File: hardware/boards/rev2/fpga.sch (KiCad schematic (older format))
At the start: 73 parts, among them J1 SD_Card, P1 CONN_02X04, P2 CONN_02X04, Q1 DNP(RE1C002UN), SW1 SW_PUSH, U6 XC7A15T-FTG256, U7 W25Q32JV

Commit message: reorganize schematic
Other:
- note added: "20 (0) mA"
- note added: "201 (1) mA"
- note added: "215 (95) mA"
- note added: "220 mA"
- note added: "3V6: 95 (78) mA\n3V3: 3 mA"
- note added: "62 (2) mA"
- note added: "62 (22) mA"
- note removed: "5 mA"
- note removed: "70 mA"
- note removed: "78 mA"
- note removed: "Iq: 1 mA\nIon: 201 mA"
- note removed: "Iq: 10 uA\nIon: 20 mA"
- note removed: "Iq: 2 mA\nIon: 62 mA"
- note removed: "Iq: 22 mA\nIon: 62 mA"
- note removed: "Iq: 95 mA\nIon: 215 mA"
- note removed: "Power-on current\n1V0: 277 mA\n1V8: 62 mA\n3V3: 296 mA\n3V6: 78 mA"
- note removed: "Quiescent current\n1V0: 97 mA\n1V8: 22 mA\n3V3: 71 mA\n3V6: 78 mA"
- moved on the sheet: C14, C15, C16, C17, C18, C19, C20, C21, C22, C23, C24, C25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

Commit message: revert to kicad v5 for pcb gen
V6 contains a few bugs and a V6 board cannot be edited with V5.
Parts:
- removed P1, P2: CONN_02X04, Connector_PinHeader_2.54mm:PinHeader_2x04_P2.54mm_Vertical_SMD, symbol Connector_Generic:Conn_02x04_Odd_Even
- added J6: Conn_02x08_Odd_Even, Connector_PinHeader_1.27mm:PinHeader_2x08_P1.27mm_Vertical, symbol Connector_Generic:Conn_02x08_Odd_Even
- U6: footprint fmcw:FTG256 -> Package_BGA:Xilinx_FTG256
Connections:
- net 3V3D: now also J6.10 (Pin_10), J6.2 (Pin_2)
- net EXT1_1: now also J6.3 (Pin_3)
- net EXT1_2: now also J6.5 (Pin_5)
- net EXT1_3: now also J6.7 (Pin_7)
- net EXT1_4: now also J6.4 (Pin_4)
- net EXT1_5: now also J6.6 (Pin_6)
- net EXT1_6: now also J6.8 (Pin_8)
- net EXT2_1: now also J6.11 (Pin_11)
- net EXT2_2: now also J6.13 (Pin_13)
- net EXT2_3: now also J6.15 (Pin_15)
- net EXT2_4: now also J6.12 (Pin_12)
- net EXT2_5: now also J6.14 (Pin_14)
- net EXT2_6: now also J6.16 (Pin_16)
- net GND: now also J6.1 (Pin_1), J6.9 (Pin_9)
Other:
- note added: "3"
- note added: "4"
- note removed: "VCCO"
- moved on the sheet: C15, C16, C20, C21, C22, C23, C24, C25, C26, C27, C28, C29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

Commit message: finish placement and routing
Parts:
- removed C15: 470n, Capacitor_SMD:C_0603_1608Metric, symbol Device:C
- J6: footprint Connector_PinHeader_1.27mm:PinHeader_2x08_P1.27mm_Vertical -> Connector_PinHeader_2.54mm:PinHeader_2x07_P2.54mm_Vertical; symbol Connector_Generic:Conn_02x08_Odd_Even -> Connector_Generic:Conn_02x07_Odd_Even
- TP1, TP2, TP3, TP4, TP5, TP6, TP7, TP8, TP9: footprint TestPoint:TestPoint_Pad_D1.0mm -> TestPoint:TestPoint_Loop_D1.80mm_Drill1.0mm_Beaded
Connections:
- net 3V3D: no longer J6.10 (Pin_10)
- net EXT2_1: now also J6.9 (Pin_9); no longer J6.11 (Pin_11)
- net EXT2_2: now also J6.11 (Pin_11); no longer J6.13 (Pin_13)
- net EXT2_3: now also J6.13 (Pin_13); no longer J6.15 (Pin_15)
- net EXT2_4: now also J6.10 (Pin_10); no longer J6.12 (Pin_12)
- net EXT2_5: now also J6.12 (Pin_12); no longer J6.14 (Pin_14)
- net EXT2_6: now also J6.14 (Pin_14); no longer J6.16 (Pin_16)
- net GND: no longer J6.9 (Pin_9)
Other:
- moved on the sheet: R10
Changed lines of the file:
@@
 	1550 14050 1550 14000
 Wire Wire Line
-	1550 14400 2100 14400
-Wire Wire Line
-	1550 14450 1550 14400
-Wire Wire Line
 	1750 10100 1550 10100
 Wire Wire Line
@@
 	2100 14300 2000 14300
 Wire Wire Line
+	2100 14400 2000 14400
+Wire Wire Line
 	2100 14500 2000 14500
 Wire Wire Line
 	2100 14600 2000 14600
 Wire Wire Line
-	2100 14700 2000 14700
-Wire Wire Line
 	2200 10300 2200 10500
 Wire Wire Line
@@
 	2600 14300 2700 14300
 Wire Wire Line
-	2600 14400 3200 14400
+	2600 14400 2700 14400
 Wire Wire Line
 	2600 14500 2700 14500
@@
 	2600 14600 2700 14600
 Wire Wire Line
-	2600 14700 2700 14700
-Wire Wire Line
 	2650 1950 2550 1950
 Wire Wire Line
@@
 	2650 6250 2400 6250
 Wire Wire Line
-	3200 14400 3200 14450
-Wire Wire Line
 	3500 14000 3500 14050
 Wire Wire Line
@@
 	5050 14750 5050 14950
 Wire Wire Line
-	6300 13850 6300 13950
+	14150 11550 14150 11650
 Wire Wire Line
 	6950 15100 6900 15100
@@
 Text Label 2000 14300 2    60   ~ 0
 EXT1_3
+Text Label 2000 14400 2    60   ~ 0
+EXT2_1
 Text Label 2000 14500 2    60   ~ 0
-EXT2_1
+EXT2_2
 Text Label 2000 14600 2    60   ~ 0
-EXT2_2
-Text Label 2000 14700 2    60   ~ 0
 EXT2_3
 Text Label 2050 10200 0    60   ~ 0
@@
 Text Label 2700 14300 0    60   ~ 0
 EXT1_6
+Text Label 2700 14400 0    60   ~ 0
+EXT2_4
 Text Label 2700 14500 0    60   ~ 0
-EXT2_4
+EXT2_5
 Text Label 2700 14600 0    60   ~ 0
-EXT2_5
-Text Label 2700 14700 0    60   ~ 0
 EXT2_6
-Text Label 3050 14400 0    60   ~ 0
-3V3D
 Text Label 3250 14000 0    60   ~ 0
 3V3D
@@
 Text Label 5050 14150 2    60   ~ 0
 PROGRAM_B
-Text Label 6300 13550 0    60   ~ 0
-3V3D
-Text Label 6300 13950 0    60   ~ 0
+Text Label 14150 11250 0    60   ~ 0
+3V3D
+Text Label 14150 11650 0    60   ~ 0
 INIT_B
 Text Label 7200 1000 0    60   ~ 0
@@
 F 0 "TP1" H 7250 2925 50  0000 C CNN
 F 1 "TestPoint" H 7250 2834 50  0000 C CNN
-F 2 "TestPoint:TestPoint_Pad_D1.0mm" H 7450 2600 50  0001 C CNN
+F 2 "TestPoint:TestPoint_Loop_D1.80mm_Drill1.0mm_Beaded" H 7450 2600 50  0001 C CNN
 F 3 "~" H 7450 2600 50  0001 C CNN
 	1    7250 2600
@@
 F 0 "TP2" H 7550 2825 50  0000 C CNN
 F 1 "TestPoint" H 7550 2734 50  0000 C CNN
-F 2 "TestPoint:TestPoint_Pad_D1.0mm" H 7750 2500 50  0001 C CNN
+F 2 "TestPoint:TestPoint_Loop_D1.80mm_Drill1.0mm_Beaded" H 7750 2500 50  0001 C CNN
 F 3 "~" H 7750 2500 50  0001 C CNN
 	1    7550 2500
@@
 F 0 "TP3" H 12300 10575 50  0000 C CNN
 F 1 "TestPoint" H 12300 10484 50  0000 C CNN
-F 2 "TestPoint:TestPoint_Pad_D1.0mm" H 12500 10250 50  0001 C CNN
+F 2 "TestPoint:TestPoint_Loop_D1.80mm_Drill1.0mm_Beaded" H 12500 10250 50  0001 C CNN
 F 3 "~" H 12500 10250 50  0001 C CNN
 	1    12300 10250
@@
 F 0 "TP4" H 12600 10675 50  0000 C CNN
 F 1 "TestPoint" H 12600 10584 50  0000 C CNN
-F 2 "TestPoint:TestPoint_Pad_D1.0mm" H 12800 10350 50  0001 C CNN
+F 2 "TestPoint:TestPoint_Loop_D1.80mm_Drill1.0mm_Beaded" H 12800 10350 50  0001 C CNN
 F 3 "~" H 12800 10350 50  0001 C CNN
 	1    12600 10350
@@
 F 0 "TP5" H 12900 10775 50  0000 C CNN
 F 1 "TestPoint" H 12900 10684 50  0000 C CNN
-F 2 "TestPoint:TestPoint_Pad_D1.0mm" H 13100 10450 50  0001 C CNN
+F 2 "TestPoint:TestPoint_Loop_D1.80mm_Drill1.0mm_Beaded" H 13100 10450 50  0001 C CNN
 F 3 "~" H 13100 10450 50  0001 C CNN
 	1    12900 10450
@@
 F 0 "TP6" H 13200 10875 50  0000 C CNN
 F 1 "TestPoint" H 13200 10784 50  0000 C CNN
-F 2 "TestPoint:TestPoint_Pad_D1.0mm" H 13400 10550 50  0001 C CNN
+F 2 "TestPoint:TestPoint_Loop_D1.80mm_Drill1.0mm_Beaded" H 13400 10550 50  0001 C CNN
 F 3 "~" H 13400 10550 50  0001 C CNN
 	1    13200 10550
@@
 F 0 "TP7" H 13250 11575 50  0000 C CNN
 F 1 "TestPoint" H 13250 11484 50  0000 C CNN
-F 2 "TestPoint:TestPoint_Pad_D1.0mm" H 13450 11250 50  0001 C CNN
+F 2 "TestPoint:TestPoint_Loop_D1.80mm_Drill1.0mm_Beaded" H 13450 11250 50  0001 C CNN
 F 3 "~" H 13450 11250 50  0001 C CNN
 	1    13250 11250
@@
 F 0 "TP8" H 13500 11075 50  0000 C CNN
 F 1 "TestPoint" H 13500 10984 50  0000 C CNN
-F 2 "TestPoint:TestPoint_Pad_D1.0mm" H 13700 10750 50  0001 C CNN
+F 2 "TestPoint:TestPoint_Loop_D1.80mm_Drill1.0mm_Beaded" H 13700 10750 50  0001 C CNN
 F 3 "~" H 13700 10750 50  0001 C CNN
 	1    13500 10750
@@
 F 0 "TP9" H 20758 4370 50  0000 L CNN
 F 1 "TestPoint" H 20758 4279 50  0000 L CNN
-F 2 "TestPoint:TestPoint_Pad_D1.0mm" H 20900 4250 50  0001 C CNN
+F 2 "TestPoint:TestPoint_Loop_D1.80mm_Drill1.0mm_Beaded" H 20900 4250 50  0001 C CNN
 F 3 "~" H 20900 4250 50  0001 C CNN
 	1    20700 4250
@@
 $EndComp
 $Comp
-L power:GND #PWR024
-U 1 1 596CB067
-P 1550 14450
-F 0 "#PWR024" H 1550 14200 50  0001 C CNN
-F 1 "GND" H 1550 14300 50  0000 C CNN
-F 2 "" H 1550 14450 60  0000 C CNN
-F 3 "" H 1550 14450 60  0000 C CNN
-	1    1550 14450
-	1    0    0    -1
-$EndComp
-$Comp
 L power:GND #PWR025
 U 1 1 5FFB0BA7
@@
 F 3 "" H 2250 12400 50  0001 C CNN
 	1    2250 12400
-	1    0    0    -1
-$EndComp
-$Comp
-L power:GND #PWR027
-U 1 1 59728463
-P 3200 14750
-F 0 "#PWR027" H 3200 14500 50  0001 C CNN
-F 1 "GND" H 3200 14600 50  0000 C CNN
-F 2 "" H 3200 14750 60  0000 C CNN
-F 3 "" H 3200 14750 60  0000 C CNN
-	1    3200 14750
 	1    0    0    -1
 $EndComp
@@
 L Device:R R10
 U 1 1 58563673
-P 6300 13700
-F 0 "R10" H 6370 13746 50  0000 L CNN
-F 1 "4.7k" H 6370 13655 50  0000 L CNN
-F 2 "Resistor_SMD:R_0402_1005Metric" V 6230 13700 30  0001 C CNN
-F 3 "" H 6300 13700 30  0000 C CNN
-F 4 "" H 2150 3900 50  0001 C CNN "MFN"
-	1    6300 13700
+P 14150 11400
+F 0 "R10" H 14220 11446 50  0000 L CNN
+F 1 "4.7k" H 14220 11355 50  0000 L CNN
+F 2 "Resistor_SMD:R_0402_1005Metric" V 14080 11400 30  0001 C CNN
+F 3 "" H 14150 11400 30  0000 C CNN
+F 4 "" H 10000 1600 50  0001 C CNN "MFN"
+	1    14150 11400
 	1    0    0    -1
 $EndComp
@@
 $EndComp
 $Comp
-L Device:C C15
-U 1 1 59727E70
-P 3200 14600
-F 0 "C15" H 3225 14700 50  0000 L CNN
-F 1 "470n" H 3225 14500 50  0000 L CNN
-F 2 "Capacitor_SMD:C_0603_1608Metric" H 3238 14450 30  0001 C CNN
-F 3 "" H 3200 14600 60  0000 C CNN
-F 4 "" H 1100 3900 50  0001 C CNN "MFN"
-	1    3200 14600
-	1    0    0    -1
-$EndComp
-$Comp
 L Device:C C16
 U 1 1 59728DD2
@@
 $EndComp
 $Comp
-L Connector_Generic:Conn_02x08_Odd_Even J6
+L Connector_Generic:Conn_02x07_Odd_Even J6
 U 1 1 5EAD300D
 P 2300 14300
 F 0 "J6" H 2350 14816 50  0000 C CNN
 F 1 "Conn_02x08_Odd_Even" H 2350 14725 50  0000 C CNN
-F 2 "Connector_PinHeader_1.27mm:PinHeader_2x08_P1.27mm_Vertical" H 2300 14300 50  0001 C CNN
+F 2 "Connector_PinHeader_2.54mm:PinHeader_2x07_P2.54mm_Vertical" H 2300 14300 50  0001 C CNN
 F 3 "~" H 2300 14300 50  0001 C CNN
 	1    2300 14300

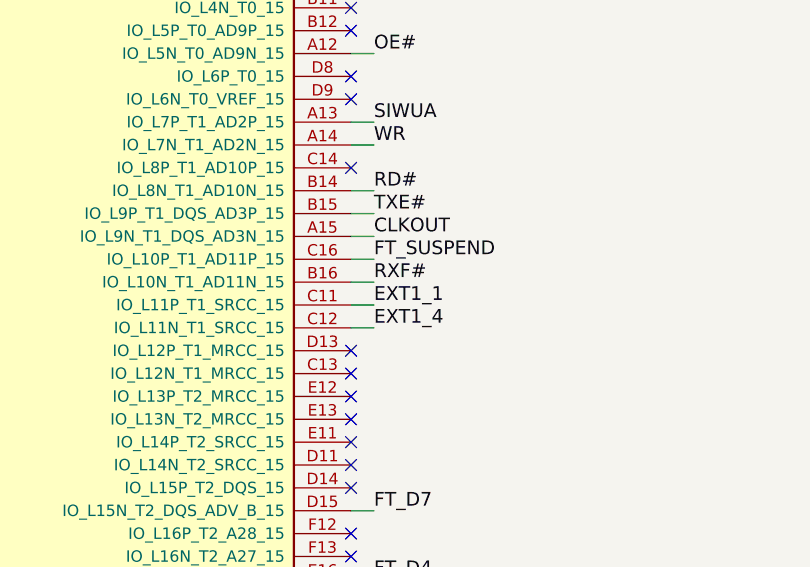
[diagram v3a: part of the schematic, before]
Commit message: switch ftclk to MRCC pin and place silkscreen
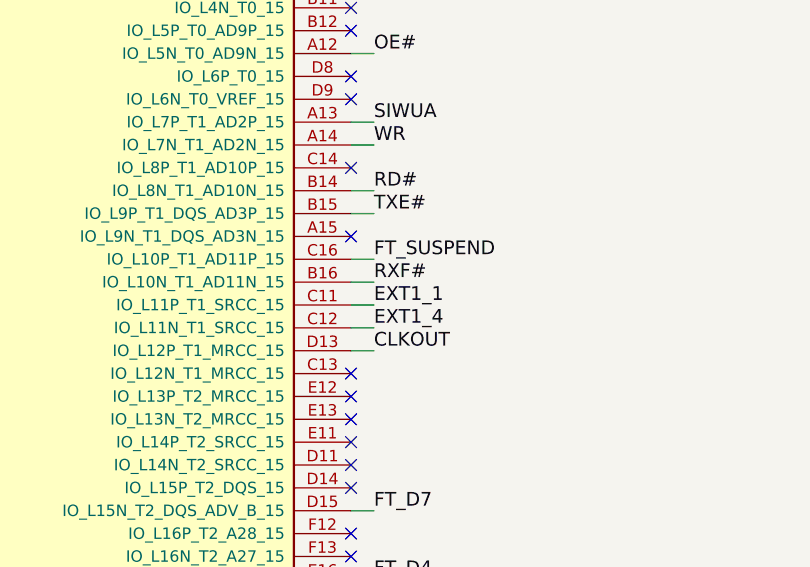
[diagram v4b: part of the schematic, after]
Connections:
- net CLKOUT: now also U6.D13 (IO_L12P_T1_MRCC_15); no longer U6.A15 (IO_L9N_T1_DQS_AD3N_15)
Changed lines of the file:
@@
 Connection ~ 7250 15300
 Connection ~ 7300 3350
-Connection ~ 11750 1700
-Connection ~ 11650 1700
-Connection ~ 11550 1700
-Connection ~ 11450 1700
-Connection ~ 11350 1700
-Connection ~ 9150 1700
-Connection ~ 9050 1700
-Connection ~ 8950 1700
-Connection ~ 8850 1700
-Connection ~ 8750 1700
 Connection ~ 16850 11850
 Connection ~ 16000 11850
@@
 NoConn ~ 12250 2500
 NoConn ~ 12250 5300
-NoConn ~ 12250 4800
 NoConn ~ 12250 5400
 NoConn ~ 12250 5200
@@
 	8550 1400 8700 1400
 Wire Wire Line
-	8650 1700 8750 1700
-Wire Wire Line
 	8700 1000 8700 1050
 Wire Wire Line
@@
 	8700 1400 8950 1400
 Wire Wire Line
-	8750 1700 8850 1700
-Wire Wire Line
-	8850 1700 8950 1700
-Wire Wire Line
 	8950 1000 8950 1050
 Wire Wire Line
 	8950 1350 8950 1400
 Wire Wire Line
-	8950 1700 9050 1700
-Wire Wire Line
-	9050 1700 9150 1700
-Wire Wire Line
-	9150 1700 11350 1700
-Wire Wire Line
 	9750 14450 9950 14450
 Wire Wire Line
@@
 	11300 14000 11300 14050
 Wire Wire Line
-	11350 1700 11450 1700
-Wire Wire Line
-	11450 1700 11550 1700
-Wire Wire Line
-	11550 1700 11650 1700
-Wire Wire Line
-	11650 1700 11750 1700
-Wire Wire Line
 	11700 9550 12050 9550
 Wire Wire Line
-	11750 1700 11850 1700
-Wire Wire Line
 	11800 1000 11800 1050
 Wire Wire Line
@@
 Wire Wire Line
 	12250 3800 12350 3800
-Wire Wire Line
-	12250 4300 12350 4300
 Wire Wire Line
 	12250 4700 12350 4700
@@
 Text Label 12350 4200 0    60   ~ 0
 TXE#
-Text Label 12350 4300 0    60   ~ 0
+Text Label 12350 4800 0    60   ~ 0
 CLKOUT
 Text Label 12350 4400 0    60   ~ 0
@@
 $Comp
 L FPGA_Xilinx_Artix7:XC7A15T-FTG256 U?
-U 1 1 5B9D6CE1
-P 10250 4600
-AR Path="/5B9D6CE1" Ref="U?"  Part="1"
-AR Path="/59395D6A/5B9D6CE1" Ref="U6"  Part="1"
-F 0 "U6" H 10250 4600 50  0000 C CNN
-F 1 "XC7A15T-FTG256" H 10250 1535 50  0000 C CNN
-F 2 "Package_BGA:Xilinx_FTG256" H 10250 4600 50  0001 C CNN
-F 3 "" H 10250 4600 50  0000 C CNN
-F 4 "XC7A15T-1FTG256C" H 3900 1100 50  0001 C CNN "MFN"
-	1    10250 4600
-	1    0    0    -1
-$EndComp
-$Comp
-L FPGA_Xilinx_Artix7:XC7A15T-FTG256 U?
 U 2 1 5CE2C3EB
 P 17800 4850
@@
 F22 "SUSPEND" O L 2650 2800 60
 $EndSheet
+Connection ~ 11750 1700
+Connection ~ 11650 1700
+Connection ~ 11550 1700
+Connection ~ 11450 1700
+Connection ~ 11350 1700
+Connection ~ 9150 1700
+Connection ~ 9050 1700
+Connection ~ 8950 1700
+Connection ~ 8850 1700
+Connection ~ 8750 1700
+Wire Wire Line
+	8650 1700 8750 1700
+Wire Wire Line
+	8750 1700 8850 1700
+Wire Wire Line
+	8850 1700 8950 1700
+Wire Wire Line
+	8950 1700 9050 1700
+Wire Wire Line
+	9050 1700 9150 1700
+Wire Wire Line
+	9150 1700 11350 1700
+Wire Wire Line
+	11350 1700 11450 1700
+Wire Wire Line
+	11450 1700 11550 1700
+Wire Wire Line
+	11550 1700 11650 1700
+Wire Wire Line
+	11650 1700 11750 1700
+Wire Wire Line
+	11750 1700 11850 1700
+$Comp
+L FPGA_Xilinx_Artix7:XC7A15T-FTG256 U?
+U 1 1 5B9D6CE1
+P 10250 4600
+AR Path="/5B9D6CE1" Ref="U?"  Part="1"
+AR Path="/59395D6A/5B9D6CE1" Ref="U6"  Part="1"
+F 0 "U6" H 10250 4600 50  0000 C CNN
+F 1 "XC7A15T-FTG256" H 10250 1535 50  0000 C CNN
+F 2 "Package_BGA:Xilinx_FTG256" H 10250 4600 50  0001 C CNN
+F 3 "" H 10250 4600 50  0000 C CNN
+F 4 "XC7A15T-1FTG256C" H 3900 1100 50  0001 C CNN "MFN"
+	1    10250 4600
+	1    0    0    -1
+$EndComp
+Wire Wire Line
+	12250 4800 12350 4800
+NoConn ~ 12250 4300
 $EndSCHEMATC
